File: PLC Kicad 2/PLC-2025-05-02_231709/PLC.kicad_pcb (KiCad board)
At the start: 2 copper layers, 75 parts, among them J1 24V, J11 Salida, J13 TB_1X2, J3 Salida, J4 Salida, J5 Salida, J6 Salida, J7 Salida, J8 Screw_Terminal_01x04, K1 RELAY_C, K2 RELAY_C, K3 RELAY_C, K4 RELAY_C, K5 RELAY_C, K6 RELAY_C, Q1 2N3904, Q10 2N3904, Q2 2N3904, Q3 2N3904, Q4 2N3904, Q5 2N3904, U1 LM2594M-5.0, U10 PC817, U11 BluePill, U12 SN74HC541PWR, U13 PC817, U2 LM2594M-3.3, U3 PC817, U4 PC817, U5 SN74HC14PWR, U6 PC817, U7 PC817, U8 PC817, U9 PC817

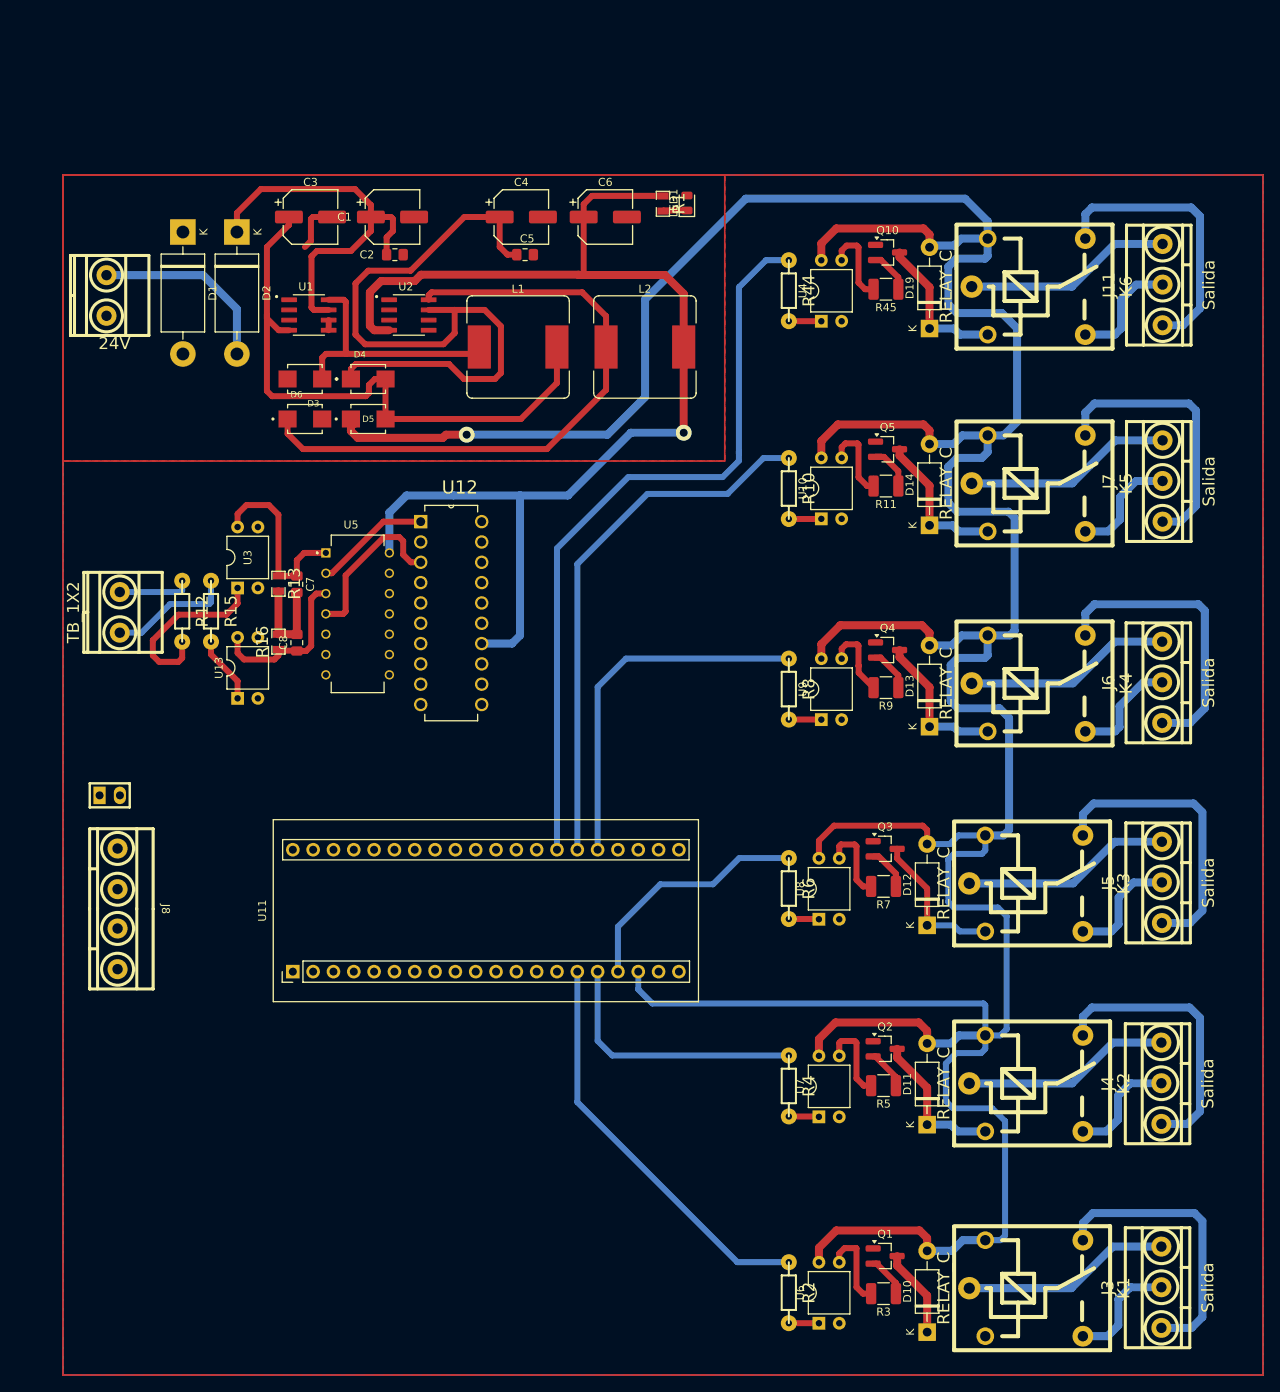
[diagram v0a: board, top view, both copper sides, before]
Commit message: Revision 0.6 (fin proto PCB)
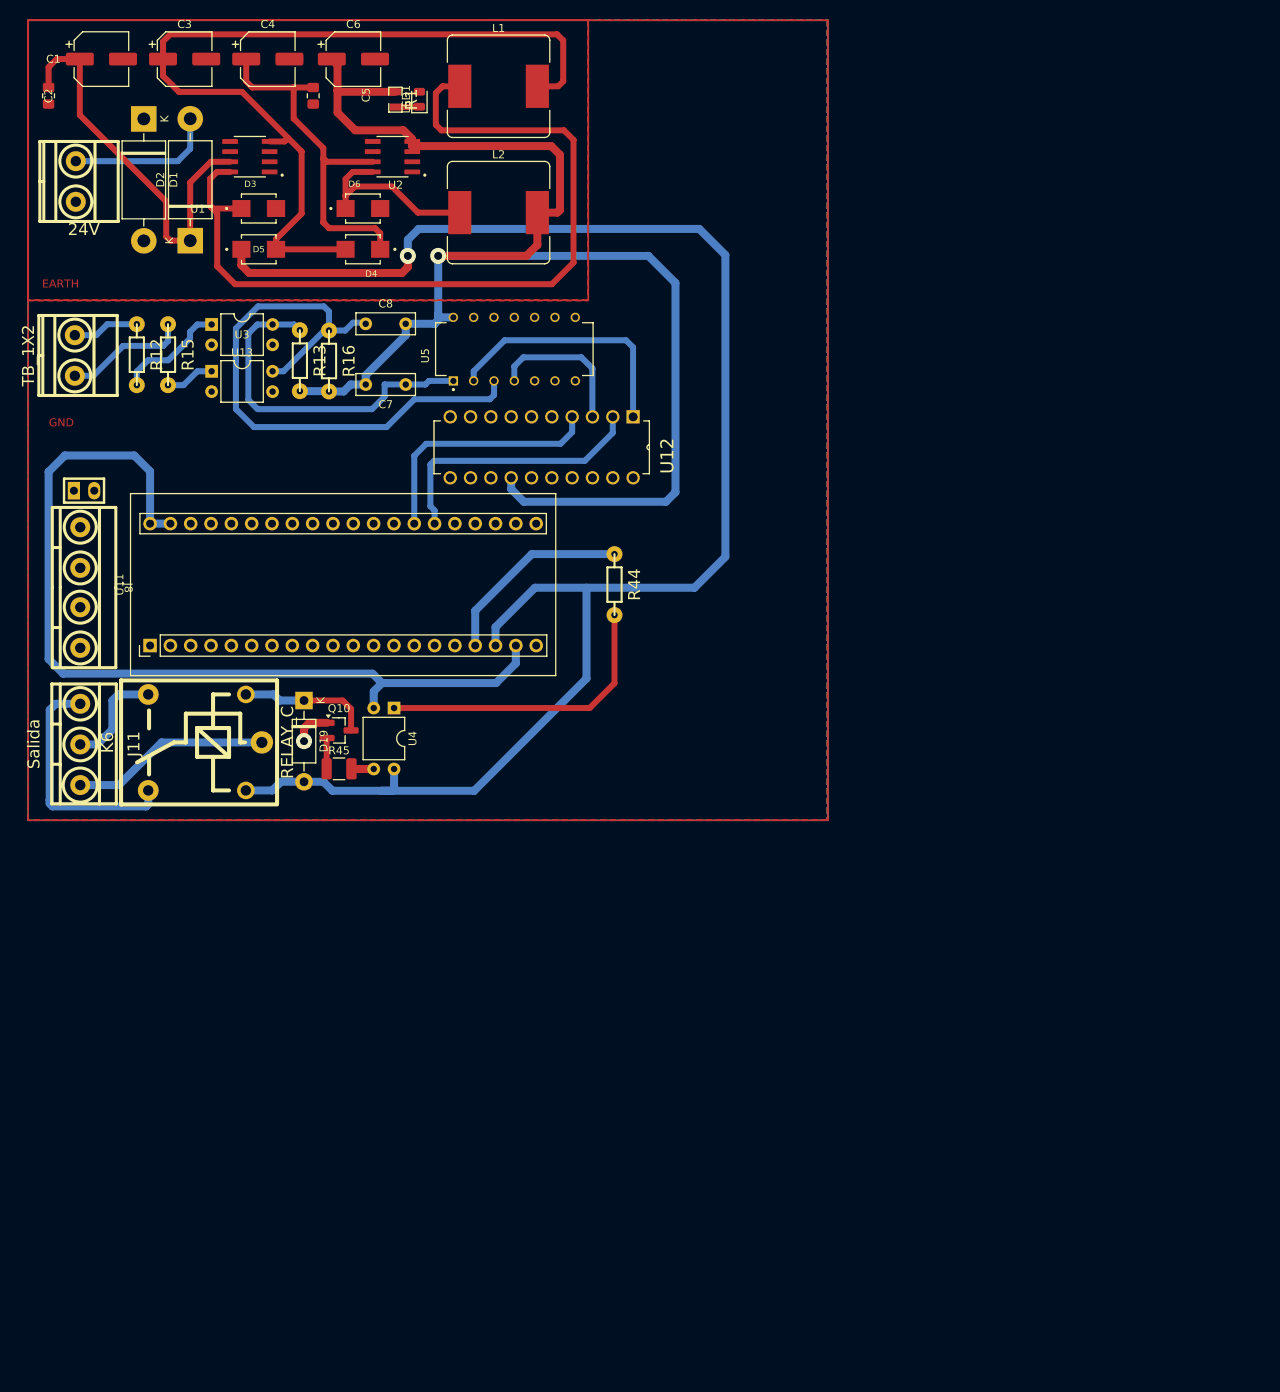
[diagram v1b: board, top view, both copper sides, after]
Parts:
- removed D10, D11, D12, D13, D14: 1N4007, Diode_THT:D_DO-41_SOD81_P10.16mm_Horizontal
- removed J3, J4, J5, J6, J7: Salida, EESTN5:BORNERA3_AZUL
- removed K1, K2, K3, K4, K5: RELAY_C, EESTN5:Relay_C
- removed Q1, Q2, Q3, Q4, Q5: 2N3904, Package_TO_SOT_SMD:SOT-23_Handsoldering
- removed R10, R2, R4, R6, R8: 220, EESTN5:RES0.3
- removed R11, R3, R5, R7, R9: 1k, Resistor_SMD:R_1210_3225Metric_Pad1.30x2.65mm_HandSolder
- removed U10, U6, U7, U8, U9: PC817, Package_DIP:DIP-4_W7.62mm
- C7, C8: value C -> 100nF; footprint Capacitor_SMD:C_0805_2012Metric_Pad1.18x1.45mm_HandSolder -> Capacitor_THT:C_Rect_L7.2mm_W2.5mm_P5.00mm_FKS2_FKP2_MKS2_MKP2
- R12, R15: value R -> 10K
- R13, R16: value R -> 10K; footprint EESTN5:R_0805 -> EESTN5:RES0.3
- moved J11 147.0 mm to (-210.4, 261.1), turned to -90 degrees
- moved K6 119.4 mm to (-195.8, 260.9), turned to -90 degrees
- moved D19 91.0 mm to (-182.4, 255.6), turned to -90 degrees
- moved Q10 90.9 mm to (-178.0, 259.4)
- moved R45 90.9 mm to (-178.0, 264.2), turned to 0 degrees
- moved U4 72.0 mm to (-171.1, 256.6), turned to -90 degrees
- moved C2 47.6 mm to (-214.3, 180.0), turned to -90 degrees
- moved U11 44.5 mm to (-201.6, 248.8)
- moved R44 42.7 mm to (-143.6, 241.1)
- moved C1 41.4 mm to (-207.7, 175.4)
- moved U13 41.0 mm to (-193.9, 214.5), turned to 0 degrees
- moved C8 40.8 mm to (-174.7, 208.5), turned to 0 degrees
- moved J8 40.4 mm to (-210.4, 241.5)
- moved U5 38.5 mm to (-156.1, 211.7), turned to 90 degrees
- moved JP1 38.2 mm to (-209.9, 229.4)
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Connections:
- R44 pad 1: /PA02 -> /PB09
- U12 pad 2: unconnected-(U12-1Y-Pad2) -> /PA01
- U12 pad 4: unconnected-(U12-2Y-Pad4) -> /PA02
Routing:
- net 5V: track 501.5 -> 205.8 mm
- net GND: track 0.00 -> 113.5 mm
- net Net-(U1-OUT): track 31.6 -> 105.4 mm
- net /PA02: track 94.6 -> 31.4 mm
- net /2A hc14: track 20.8 -> 76.3 mm
- net Net-(U2-OUT): track 78.9 -> 23.6 mm
- net /PB07: track 51.0 -> 0.00 mm
- net /PA0: track 45.7 -> 0.00 mm
- net Net-(U2-VIN): track 87.6 -> 45.9 mm
- net Net-(J6-Pin_1): track 36.8 -> 0.00 mm
- net Net-(J5-Pin_1): track 36.6 -> 0.00 mm
- net Net-(J3-Pin_1): track 35.7 -> 0.00 mm
- net Net-(J4-Pin_1): track 35.2 -> 0.00 mm
- net Net-(J7-Pin_1): track 34.4 -> 0.00 mm
- net /PA01: track 67.6 -> 34.1 mm
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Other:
- board text added: "EARTH"
- board text added: "GND"

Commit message: Revision 0.7 (BUCKS)
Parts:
- removed the C7 at (-169.7, 216.1)
- removed the C8 at (-174.7, 208.5)
- removed the D19 at (-182.4, 255.6)
- removed the J11 at (-210.4, 261.1)
- removed the J13 at (-211.1, 212.5)
- removed the J8 at (-210.4, 241.5)
- removed the JP1 at (-209.9, 229.4)
- removed the K6 at (-195.8, 260.9)
- removed the Q10 at (-178.0, 259.4)
- removed the R12 at (-203.3, 212.4)
- removed the R13 at (-182.9, 213.2)
- removed the R15 at (-199.4, 212.4)
- removed the R16 at (-179.3, 213.2)
- removed the R44 at (-143.6, 241.1)
- removed the R45 at (-178.0, 264.2)
- removed the U11 at (-201.6, 248.8)
- removed the U12 at (-164.1, 227.8)
- removed the U13 at (-193.9, 214.5)
- removed the U3 at (-193.9, 208.6)
- removed the U4 at (-171.1, 256.6)
- removed the U5 at (-156.1, 211.7)
- added C7: 100nF, Capacitor_THT:C_Rect_L7.2mm_W2.5mm_P5.00mm_FKS2_FKP2_MKS2_MKP2, F.Cu at (229.9, 68.3)
- added C7: 100nF, Capacitor_THT:C_Rect_L7.2mm_W2.5mm_P5.00mm_FKS2_FKP2_MKS2_MKP2, F.Cu at (88.4, 66.5)
- added C8: 100nF, Capacitor_THT:C_Rect_L7.2mm_W2.5mm_P5.00mm_FKS2_FKP2_MKS2_MKP2, F.Cu at (224.9, 60.7)
- added C8: 100nF, Capacitor_THT:C_Rect_L7.2mm_W2.5mm_P5.00mm_FKS2_FKP2_MKS2_MKP2, F.Cu at (83.4, 59.0)
- added D19: 1N4007, Diode_THT:D_DO-41_SOD81_P10.16mm_Horizontal, F.Cu at (217.2, 107.8)
- added D19: 1N4007, Diode_THT:D_DO-41_SOD81_P10.16mm_Horizontal, F.Cu at (75.7, 106.0)
- added F1: Fuse, EESTN5:Fusible2, F.Cu at (256.0, 37.2)
- added F1: Fuse, EESTN5:Fusible2, F.Cu at (81.1, 10.7)
- added J11: Salida, EESTN5:BORNERA3_AZUL, F.Cu at (189.3, 113.3)
- added J11: Salida, EESTN5:BORNERA3_AZUL, F.Cu at (47.7, 111.5)
- added J13: TB_1X2, EESTN5:BORNERA2, F.Cu at (188.6, 64.7)
- added J13: TB_1X2, EESTN5:BORNERA2, F.Cu at (47.0, 62.9)
- added J14: TB_1X2, EESTN5:BORNERA2, F.Cu at (62.8, 27.4)
- added J15: TB_1X2, EESTN5:BORNERA2, F.Cu at (77.7, 27.4)
- added J16: TB_1X2, EESTN5:BORNERA2, F.Cu at (47.2, 31.8)
- added J17: TB_1X2, EESTN5:BORNERA2, F.Cu at (47.2, 48.3)
- added J8: Screw_Terminal_01x04, Library:Bornera_4, F.Cu at (189.3, 93.7)
- added J8: Screw_Terminal_01x04, Library:Bornera_4, F.Cu at (47.7, 91.9)
- added JP1: Jumper, EESTN5:Jumper_Alto, F.Cu at (189.5, 80.7)
- added JP1: Jumper, EESTN5:Jumper_Alto, F.Cu at (47.9, 78.9)
- added K6: RELAY_C, EESTN5:Relay_C, F.Cu at (203.9, 113.0)
- added K6: RELAY_C, EESTN5:Relay_C, F.Cu at (62.3, 111.3)
- added Q10: 2N3904, Package_TO_SOT_SMD:SOT-23_Handsoldering, F.Cu at (80.0, 109.8)
- added Q10: 2N3904, Package_TO_SOT_SMD:SOT-23_Handsoldering, F.Cu at (221.6, 111.5)
- added R12: 10K, EESTN5:RES0.3, F.Cu at (196.3, 64.6)
- added R12: 10K, EESTN5:RES0.3, F.Cu at (54.8, 62.8)
- added R13: 10K, EESTN5:RES0.3, F.Cu at (216.7, 65.3)
- added R13: 10K, EESTN5:RES0.3, F.Cu at (75.1, 63.6)
- added R15: 10K, EESTN5:RES0.3, F.Cu at (200.2, 64.6)
- added R15: 10K, EESTN5:RES0.3, F.Cu at (58.7, 62.8)
- added R16: 10K, EESTN5:RES0.3, F.Cu at (220.3, 65.3)
- added R16: 10K, EESTN5:RES0.3, F.Cu at (78.8, 63.6)
- added R44: 220, EESTN5:RES0.3, F.Cu at (256.0, 93.3)
- added R44: 220, EESTN5:RES0.3, F.Cu at (114.5, 91.6)
- added R45: 1k, Resistor_SMD:R_1210_3225Metric_Pad1.30x2.65mm_HandSolder, F.Cu at (221.6, 116.3)
- added R45: 1k, Resistor_SMD:R_1210_3225Metric_Pad1.30x2.65mm_HandSolder, F.Cu at (80.0, 114.6)
- added U11: BluePill, EESTN5:BluePill, F.Cu at (56.4, 99.2)
- added U11: BluePill, EESTN5:BluePill, F.Cu at (198.0, 100.9)
- added U12: SN74HC541PWR, SN74HC541N:DIP254P762X508-20, F.Cu at (235.5, 80.0)
- added U12: SN74HC541PWR, SN74HC541N:DIP254P762X508-20, F.Cu at (93.9, 78.2)
- added U13: PC817, Package_DIP:DIP-4_W7.62mm, F.Cu at (205.7, 66.6)
- added U13: PC817, Package_DIP:DIP-4_W7.62mm, F.Cu at (64.1, 64.9)
- added U3: PC817, Package_DIP:DIP-4_W7.62mm, F.Cu at (64.1, 59.0)
- added U3: PC817, Package_DIP:DIP-4_W7.62mm, F.Cu at (205.7, 60.8)
- added U4: PC817, Package_DIP:DIP-4_W7.62mm, F.Cu at (228.5, 108.7)
- added U4: PC817, Package_DIP:DIP-4_W7.62mm, F.Cu at (86.9, 107.0)
- added U5: SN74HC14PWR, SN74HC14N:DIP794W45P254L1969H508Q14, F.Cu at (243.5, 63.9)
- added U5: SN74HC14PWR, SN74HC14N:DIP794W45P254L1969H508Q14, F.Cu at (102.0, 62.1)
- moved C1 426.1 mm to (191.9, 27.6)
- moved C2 426.1 mm to (185.3, 32.2)
- moved C3 426.1 mm to (202.3, 27.6)
- moved C4 426.1 mm to (212.7, 27.6)
- moved C5 426.1 mm to (218.4, 32.2)
- moved C6 426.1 mm to (223.4, 27.6)
- moved D1 426.1 mm to (197.2, 35.1)
- moved D2 426.1 mm to (203.0, 50.3)
- moved D3 426.1 mm to (211.6, 46.3)
- moved D4 426.1 mm to (224.6, 51.4)
- moved D5 426.1 mm to (211.6, 51.4)
- moved D6 426.1 mm to (224.6, 46.3)
- moved J1 426.1 mm to (188.7, 42.9)
- moved L1 426.1 mm to (241.6, 31.0)
- moved L2 426.1 mm to (241.6, 46.8)
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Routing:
- net 5V: track 205.8 -> 442.8 mm
- net /VCC: track 184.6 -> 343.6 mm
- net GND: track 113.5 -> 227.7 mm
- net Net-(J8-Pin_2): track 0.00 -> 86.4 mm
- net /2A hc14: track 76.3 -> 152.7 mm
- net Net-(D2-A): track 0.00 -> 68.0 mm, vias 0 -> 1
- net Net-(F1-Pad1): track 18.7 -> 81.5 mm, vias 0 -> 1
- net Net-(J8-Pin_3): track 0.00 -> 55.4 mm
- net /1A hc14: track 44.2 -> 88.3 mm
- net Net-(R44-Pad2): track 37.4 -> 74.7 mm
- net /PA01: track 34.1 -> 68.1 mm
- net /1Y hc14: track 31.8 -> 63.6 mm
- net /PA02: track 31.4 -> 62.7 mm
- net Net-(J11-Pin_1): track 29.0 -> 58.0 mm
- net Net-(J11-Pin_3): track 24.9 -> 49.8 mm
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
